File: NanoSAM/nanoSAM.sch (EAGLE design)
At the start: 102 parts, among them J1 POWER_JACK, U1 LTC3260EMSEPBF, U2 LMV324

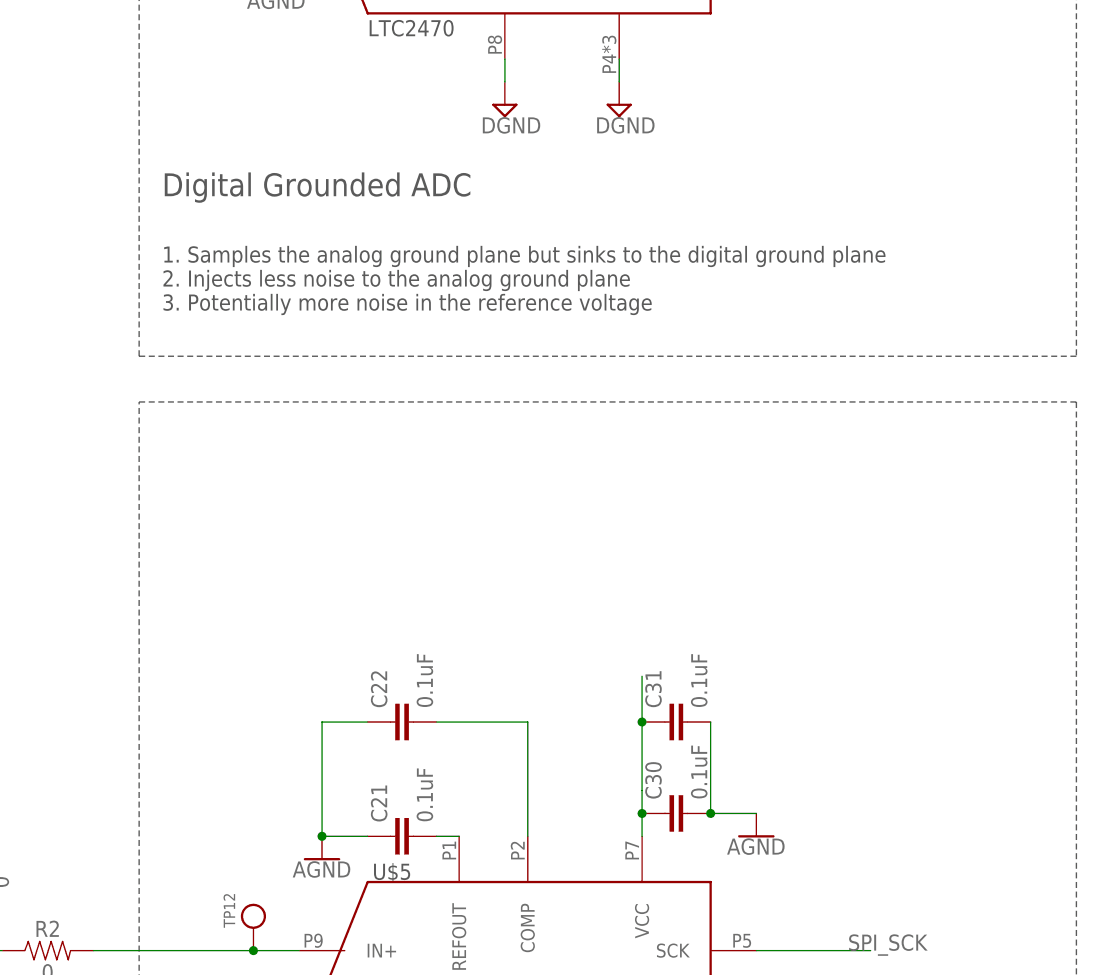
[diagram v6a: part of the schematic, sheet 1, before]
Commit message: Added analog grounded ADC power regulator
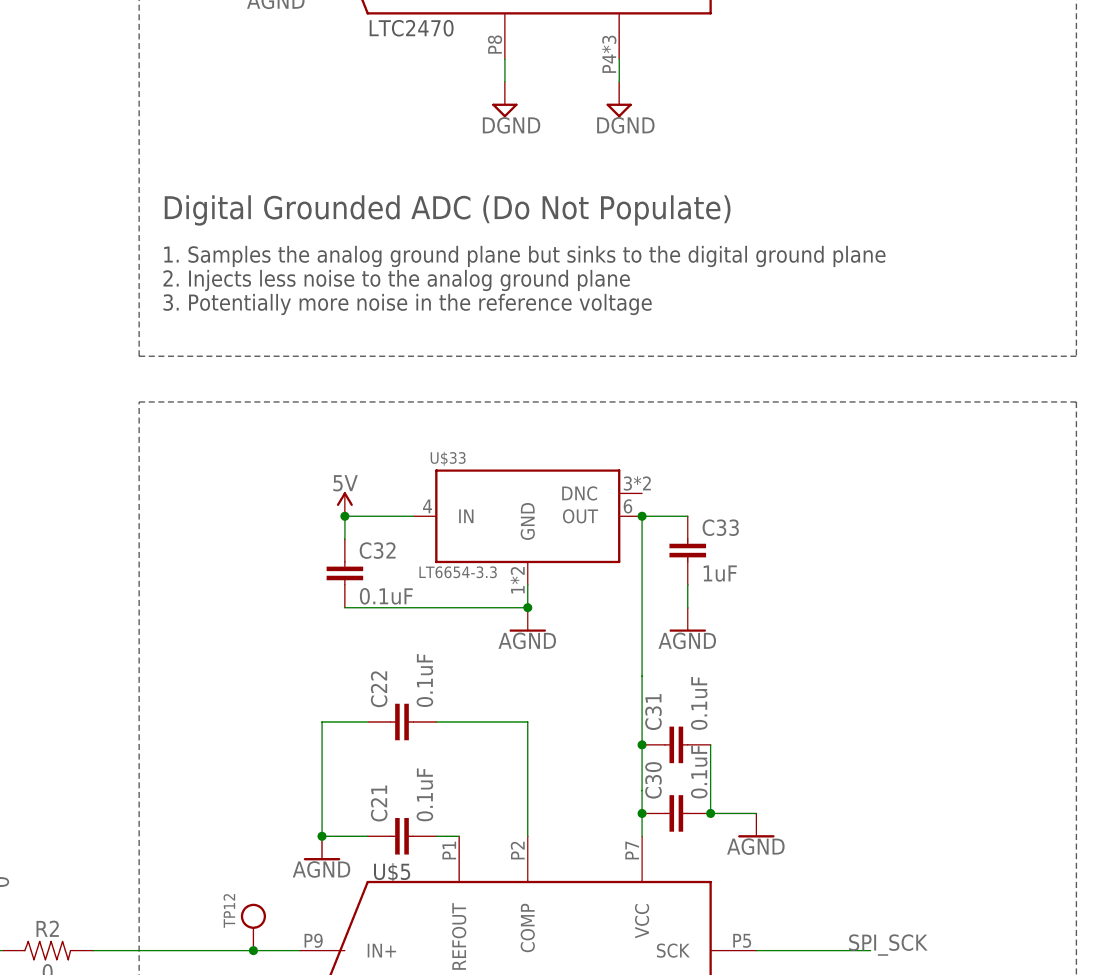
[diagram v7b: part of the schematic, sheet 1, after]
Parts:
- added C32: 0.1uF, SparkFun-Capacitors:0.1UF-0603-25V-5%
- added C33: 1uF, SparkFun-Capacitors:0.1UF-0603-25V-5%
- added U$33: LT6654-3.3, LT6654:LT6654-3.3
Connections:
- net 5V: now also C32.1, U$33.IN
- net AGND: now also C32.2, C33.2, U$33.GND
- net N$26: now also C33.1, U$33.OUT
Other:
- note added: "Digital Grounded ADC (Do Not Populate)"
- note removed: "Digital Grounded ADC"
- moved on the sheet: C31
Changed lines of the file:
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@@
 <part name="U$32" library="SparkFun-PowerSymbols" library_urn="urn:adsk.eagle:library:530" deviceset="AGND" device=""/>
 <part name="R1" library="SparkFun-Resistors" library_urn="urn:adsk.eagle:library:532" deviceset="RESISTOR" device="0805" package3d_urn="urn:adsk.eagle:package:39651/1" value="0"/>
+<part name="U$33" library="LT6654" deviceset="LT6654-3.3" device=""/>
+<part name="SUPPLY39" library="SparkFun-PowerSymbols" library_urn="urn:adsk.eagle:library:530" deviceset="5V" device=""/>
+<part name="C32" library="SparkFun-Capacitors" library_urn="urn:adsk.eagle:library:510" deviceset="0.1UF" device="-0603-25V-5%" package3d_urn="urn:adsk.eagle:package:37414/1" value="0.1uF"/>
+<part name="C33" library="SparkFun-Capacitors" library_urn="urn:adsk.eagle:library:510" deviceset="0.1UF" device="-0603-25V-5%" package3d_urn="urn:adsk.eagle:package:37414/1" value="1uF"/>
+<part name="U$34" library="SparkFun-PowerSymbols" library_urn="urn:adsk.eagle:library:530" deviceset="AGND" device=""/>
+<part name="U$35" library="SparkFun-PowerSymbols" library_urn="urn:adsk.eagle:library:530" deviceset="AGND" device=""/>
 </parts>
 <sheets>
@@
 2. Powered from analog power supply
 3. May inject some noise into analog ground plane</text>
-<text x="129.54" y="114.3" size="2.54" layer="97">Digital Grounded ADC</text>
+<text x="129.54" y="111.76" size="2.54" layer="97">Digital Grounded ADC (Do Not Populate)</text>
 <text x="129.54" y="101.6" size="1.778" layer="97">1. Samples the analog ground plane but sinks to the digital ground plane
 2. Injects less noise to the analog ground plane
@@
 <attribute name="VALUE" x="190.119" y="47.244" size="1.778" layer="96" font="vector" rot="R90"/>
 </instance>
-<instance part="C31" gate="G$1" x="187.96" y="55.88" smashed="yes" rot="R90">
-<attribute name="NAME" x="185.039" y="57.404" size="1.778" layer="95" font="vector" rot="R90"/>
-<attribute name="VALUE" x="190.119" y="57.404" size="1.778" layer="96" font="vector" rot="R90"/>
+<instance part="C31" gate="G$1" x="187.96" y="53.34" smashed="yes" rot="R90">
+<attribute name="NAME" x="185.039" y="54.864" size="1.778" layer="95" font="vector" rot="R90"/>
+<attribute name="VALUE" x="190.119" y="54.864" size="1.778" layer="96" font="vector" rot="R90"/>
 </instance>
 <instance part="U$27" gate="G$1" x="142.24" y="15.24" smashed="yes">
@@
 <attribute name="NAME" x="107.696" y="38.1" size="1.778" layer="95" font="vector" rot="R90" align="bottom-center"/>
 <attribute name="VALUE" x="110.744" y="38.1" size="1.778" layer="96" font="vector" rot="R90" align="top-center"/>
+</instance>
+<instance part="U$33" gate="G$1" x="170.18" y="78.74" smashed="yes">
+<attribute name="NAME" x="159.258" y="84.582" size="1.27" layer="95"/>
+<attribute name="VALUE" x="157.988" y="71.882" size="1.27" layer="96"/>
+</instance>
+<instance part="SUPPLY39" gate="G$1" x="149.86" y="78.74" smashed="yes">
+<attribute name="VALUE" x="149.86" y="81.534" size="1.778" layer="96" align="bottom-center"/>
+</instance>
+<instance part="C32" gate="G$1" x="149.86" y="71.12" smashed="yes">
+<attribute name="NAME" x="151.384" y="74.041" size="1.778" layer="95" font="vector"/>
+<attribute name="VALUE" x="151.384" y="68.961" size="1.778" layer="96" font="vector"/>
+</instance>
+<instance part="C33" gate="G$1" x="187.96" y="73.66" smashed="yes">
+<attribute name="NAME" x="189.484" y="76.581" size="1.778" layer="95" font="vector"/>
+<attribute name="VALUE" x="189.484" y="71.501" size="1.778" layer="96" font="vector"/>
+</instance>
+<instance part="U$34" gate="G$1" x="170.18" y="66.04" smashed="yes">
+<attribute name="VALUE" x="170.18" y="65.786" size="1.778" layer="96" align="top-center"/>
+</instance>
+<instance part="U$35" gate="G$1" x="187.96" y="66.04" smashed="yes">
+<attribute name="VALUE" x="187.96" y="65.786" size="1.778" layer="96" align="top-center"/>
 </instance>
 </instances>
@@
 <junction x="71.12" y="50.8"/>
 </segment>
+<segment>
+<pinref part="U$33" gate="G$1" pin="IN"/>
+<pinref part="SUPPLY39" gate="G$1" pin="5V"/>
+<wire x1="157.48" y1="78.74" x2="149.86" y2="78.74" width="0.1524" layer="91"/>
+<pinref part="C32" gate="G$1" pin="1"/>
+<wire x1="149.86" y1="76.2" x2="149.86" y2="78.74" width="0.1524" layer="91"/>
+<junction x="149.86" y="78.74"/>
+</segment>
 </net>
 <net name="AGND" class="0">
@@
 <pinref part="C31" gate="G$1" pin="2"/>
 <pinref part="C30" gate="G$1" pin="2"/>
-<wire x1="190.5" y1="55.88" x2="190.5" y2="45.72" width="0.1524" layer="91"/>
+<wire x1="190.5" y1="53.34" x2="190.5" y2="45.72" width="0.1524" layer="91"/>
 <wire x1="190.5" y1="45.72" x2="195.58" y2="45.72" width="0.1524" layer="91"/>
 <junction x="190.5" y="45.72"/>
@@
 <pinref part="U$32" gate="G$1" pin="AGND"/>
 <junction x="147.32" y="43.18"/>
+</segment>
+<segment>
+<pinref part="C33" gate="G$1" pin="2"/>
+<pinref part="U$35" gate="G$1" pin="AGND"/>
+<wire x1="187.96" y1="71.12" x2="187.96" y2="68.58" width="0.1524" layer="91"/>
+</segment>
+<segment>
+<pinref part="U$34" gate="G$1" pin="AGND"/>
+<pinref part="C32" gate="G$1" pin="2"/>
+<wire x1="170.18" y1="68.58" x2="149.86" y2="68.58" width="0.1524" layer="91"/>
+<pinref part="U$33" gate="G$1" pin="GND"/>
+<wire x1="170.18" y1="71.12" x2="170.18" y2="68.58" width="0.1524" layer="91"/>
+<junction x="170.18" y="68.58"/>
 </segment>
 </net>
@@
 <junction x="182.88" y="45.72"/>
 <pinref part="C31" gate="G$1" pin="1"/>
-<wire x1="182.88" y1="55.88" x2="182.88" y2="48.26" width="0.1524" layer="91"/>
-<wire x1="182.88" y1="60.96" x2="182.88" y2="55.88" width="0.1524" layer="91"/>
-<junction x="182.88" y="55.88"/>
-</segment>
-</net>
+<wire x1="182.88" y1="53.34" x2="182.88" y2="48.26" width="0.1524" layer="91"/>
+<wire x1="182.88" y1="60.96" x2="182.88" y2="53.34" width="0.1524" layer="91"/>
+<junction x="182.88" y="53.34"/>
+<pinref part="U$33" gate="G$1" pin="OUT"/>
+<wire x1="182.88" y1="78.74" x2="182.88" y2="60.96" width="0.1524" layer="91"/>
+<pinref part="C33" gate="G$1" pin="1"/>
+<wire x1="187.96" y1="78.74" x2="182.88" y2="78.74" width="0.1524" layer="91"/>
+<junction x="182.88" y="78.74"/>
+</segment>
+</net>

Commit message: Finished fixing stuff
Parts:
- added R28, R31, R37, R38, R39, R5: 49.99, SparkFun-Resistors:RESISTOR0805
- C25, C26: value 47uF -> 47uF - 10V
- R22: value 230k -> 240k
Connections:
- removed net 6V_PWR_ENA: U$12.EN/UV
- removed net N$43: U$12.NC
- removed net PWR_6V_PG: U$12.PG
- new net HK_3V3_PG: U$12.PG, U$2.D0
- new net N$30: R5.1, U$5.SDO
- new net N$33: R28.1, U$26.SDO
- new net N$38: R31.2, U$2.D11
- new net N$39: R37.1, U$2.D13/LED
- new net N$40: R38.2, U$16.SO
- new net N$41: R39.2, U$17.SO
- net DGND: now also U$12.NC, U$2.AGND
- net N$84: now also U$12.EN/UV
- net SPI_MISO: now also R28.2, R38.1, R39.1, R5.2; no longer U$16.SO, U$17.SO, U$26.SDO, U$5.SDO
- net SPI_MOSI: now also R31.1; no longer U$2.D11
- net SPI_SCK: now also R37.2; no longer U$2.D13/LED
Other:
- moved on the sheet: C15, C3, R30, R4, U$16, U$17
